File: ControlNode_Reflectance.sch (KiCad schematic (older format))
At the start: 8 parts, among them P5 TE_640456-8, P6 TE_640456-8, P7 TE_640456-8, U8 SN74HCT14PWR

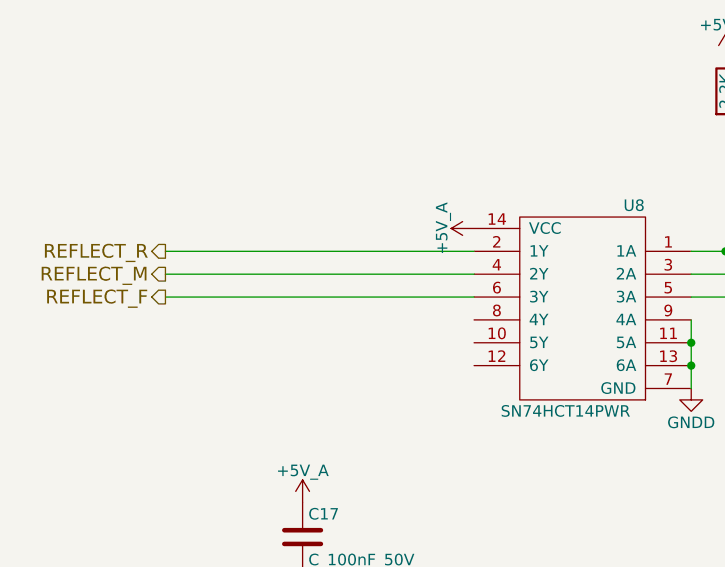
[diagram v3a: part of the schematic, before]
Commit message: Fix reflectance voltage levels and print sch for design review.
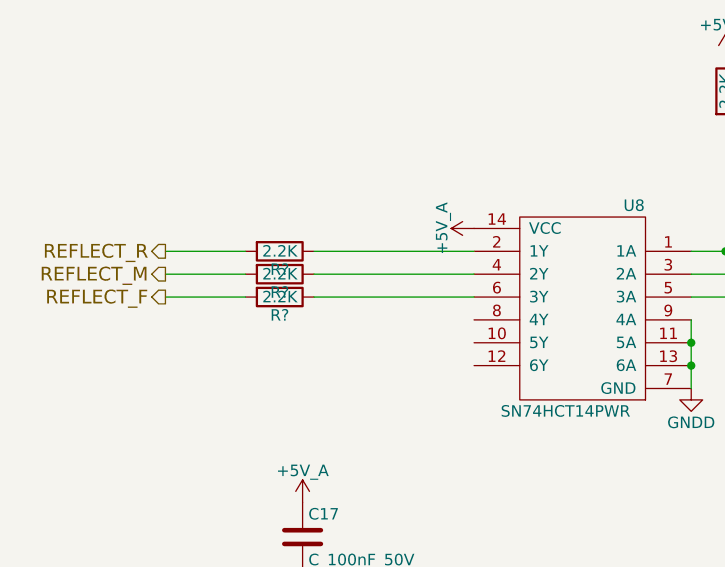
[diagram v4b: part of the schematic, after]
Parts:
- added R? (x3): 2.2K, RLOOP_FOOTPRINTS:rLoop_R_0603, symbol 2.2K
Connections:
- wire segments 41 -> 44
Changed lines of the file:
@@
 FRONT_SIG_Q1
-Wire Wire Line
-	7050 2500 5700 2500
-Wire Wire Line
-	7050 2600 5700 2600
-Wire Wire Line
-	7050 2700 5700 2700
 Wire Wire Line
 	8000 2800 8000 3100
 Connection ~ 8000 2900
 Connection ~ 8000 3000
+$Comp
+L 2.2K R?
+U 1 1 5769813D
+P 6200 2500
+F 0 "R?" V 6280 2500 50  0000 C CNN
+F 1 "2.2K" V 6200 2500 50  0000 C CNN
+F 2 "RLOOP_FOOTPRINTS:rLoop_R_0603" V 6130 2500 50  0001 C CNN
+F 3 "" H 6200 2500 50  0000 C CNN
+	1    6200 2500
+	0    1    1    0
+$EndComp
+$Comp
+L 2.2K R?
+U 1 1 576981DD
+P 6200 2600
+F 0 "R?" V 6280 2600 50  0000 C CNN
+F 1 "2.2K" V 6200 2600 50  0000 C CNN
+F 2 "RLOOP_FOOTPRINTS:rLoop_R_0603" V 6130 2600 50  0001 C CNN
+F 3 "" H 6200 2600 50  0000 C CNN
+	1    6200 2600
+	0    1    1    0
+$EndComp
+$Comp
+L 2.2K R?
+U 1 1 576981F3
+P 6200 2700
+F 0 "R?" V 6280 2700 50  0000 C CNN
+F 1 "2.2K" V 6200 2700 50  0000 C CNN
+F 2 "RLOOP_FOOTPRINTS:rLoop_R_0603" V 6130 2700 50  0001 C CNN
+F 3 "" H 6200 2700 50  0000 C CNN
+	1    6200 2700
+	0    1    1    0
+$EndComp
+Wire Wire Line
+	7050 2500 6350 2500
+Wire Wire Line
+	6350 2600 7050 2600
+Wire Wire Line
+	7050 2700 6350 2700
+Wire Wire Line
+	6050 2500 5700 2500
+Wire Wire Line
+	5700 2600 6050 2600
+Wire Wire Line
+	6050 2700 5700 2700
 $EndSCHEMATC
